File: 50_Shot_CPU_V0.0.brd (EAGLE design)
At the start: 86 x 100 mm, 74 parts, among them IC1 PIC24FJ128GA010, J1 J12, J10 22-23-2021, J11 22-23-2061, J12 A311422_nd, J13 22-23-2021, J14 22-23-2021, J3 22-23-2021, J4 22-23-2021, J5 22-23-2021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

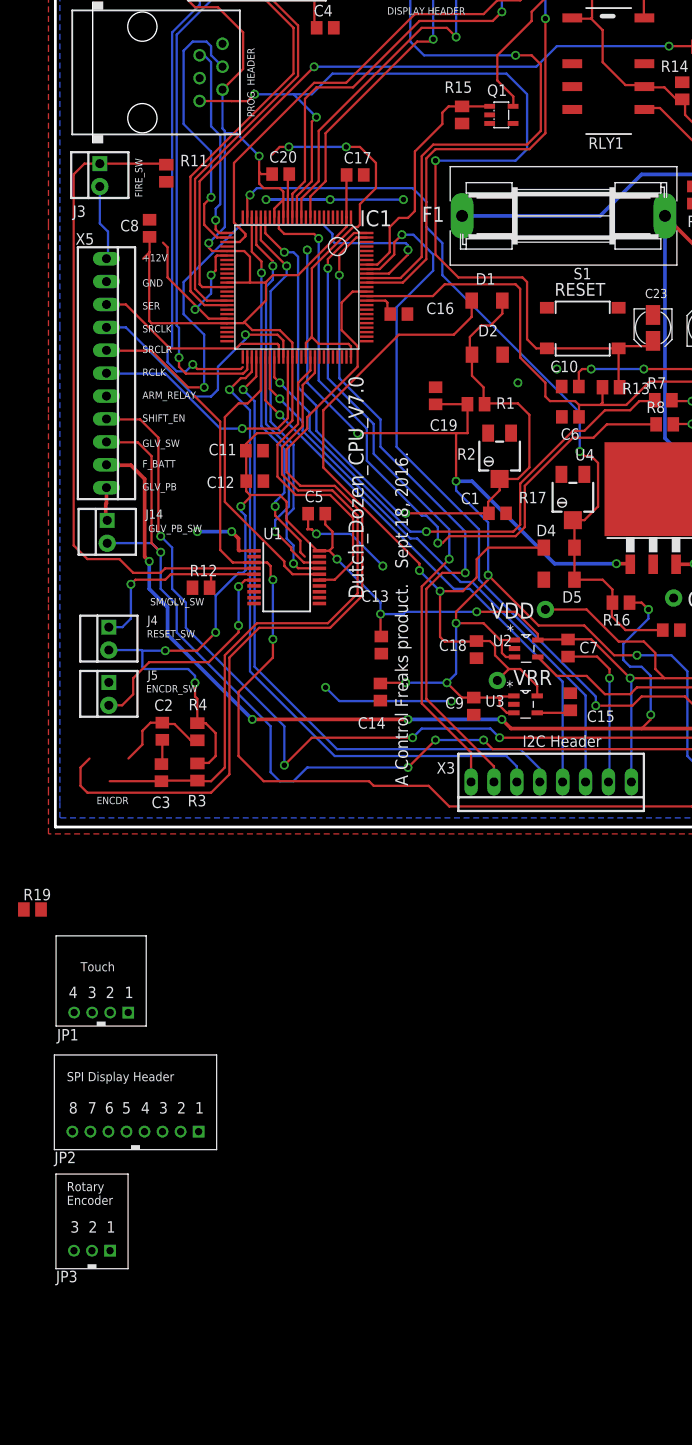
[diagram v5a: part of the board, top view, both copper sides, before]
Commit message: converted programming header
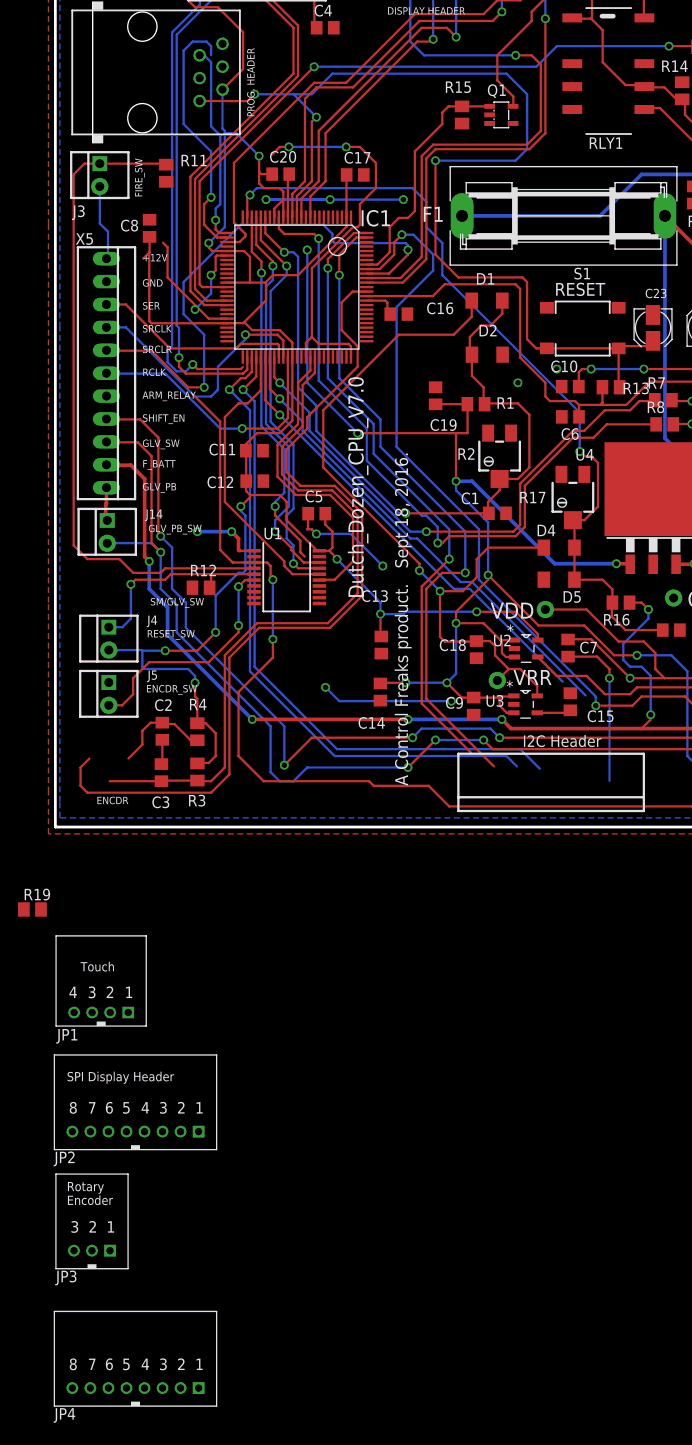
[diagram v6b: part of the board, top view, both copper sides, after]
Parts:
- removed X3: 22-23-2081, con-molex:22-23-2081
- added JP4: SHERLOCK_8PIN_RGT, Mine:SHERLOCK_8PIN-RGT
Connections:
- net 2PG_C renamed RB6_2PG_C
- net 2PG_D renamed RB7_2PG_D
- removed net SCL1-RG2: IC1.57, X3.6
- removed net SDA1-RG3: IC1.56, X3.5
- removed net VSS: C7.2, X3.7
- new net RG2_SCL1: IC1.57, JP4.6
- new net RG3_SDA1: IC1.56, JP4.5
- net GND: now also JP4.7
- net RE3: now also C7.2, JP4.2; no longer X3.2
- net RE4: now also C7.1, JP4.1; no longer X3.1
- net RF7: now also JP4.4; no longer X3.4
- net RF8: now also JP4.3; no longer X3.3
- net VDD: now also JP4.8; no longer C7.1, X3.8
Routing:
- net SCL1-RG2: track 62.8 -> 0.00 mm, vias 1 -> 0
- net SDA1-RG3: track 61.8 -> 0.00 mm, vias 1 -> 0
- net RG2_SCL1: track 0.00 -> 53.2 mm, vias 0 -> 1
- net RG3_SDA1: track 0.00 -> 50.7 mm, vias 0 -> 1
- net VSS: track 17.7 -> 0.00 mm, vias 1 -> 0
- net RE3: track 74.5 -> 90.4 mm, vias 2 -> 3
- net VDD: track 407.4 -> 392.7 mm
- net RE4: track 72.6 -> 69.4 mm
- net RB7_2PG_D: track 30.8 -> 29.0 mm
- net RF8: track 72.8 -> 71.1 mm
- net RF7: track 73.3 -> 71.8 mm

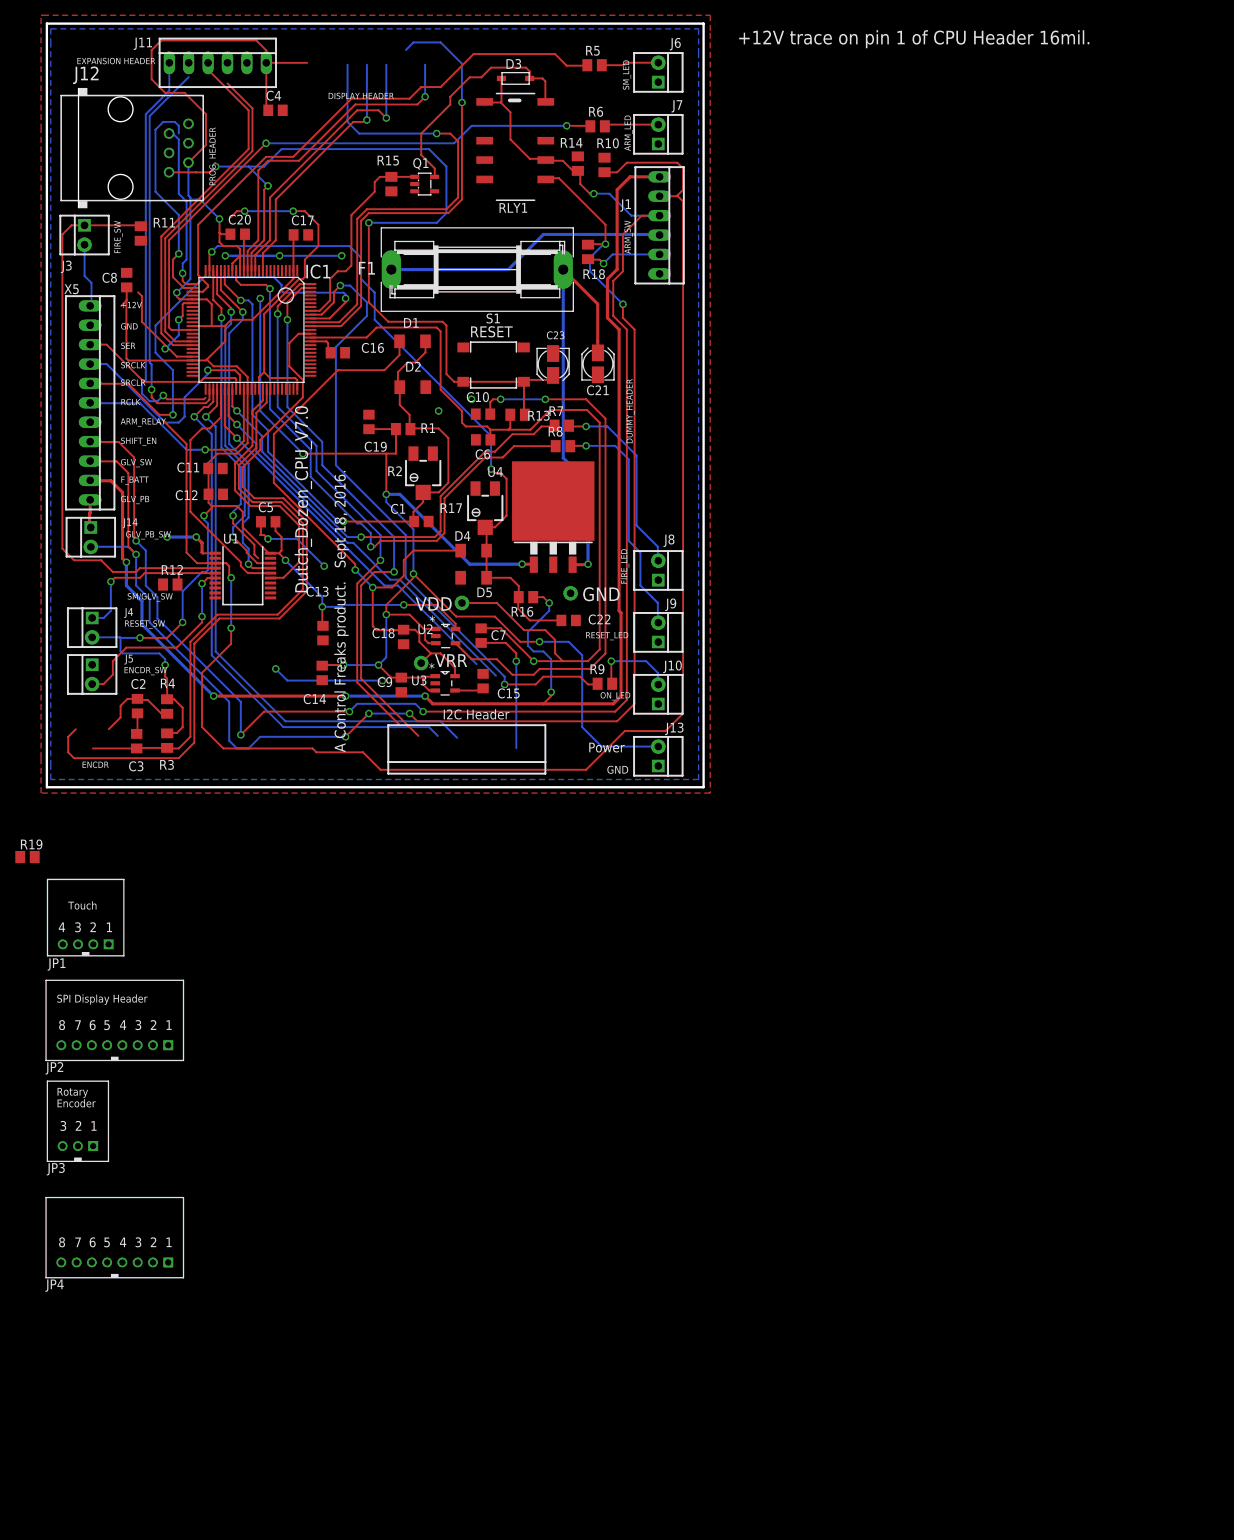
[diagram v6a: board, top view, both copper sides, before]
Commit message: converted LED headers
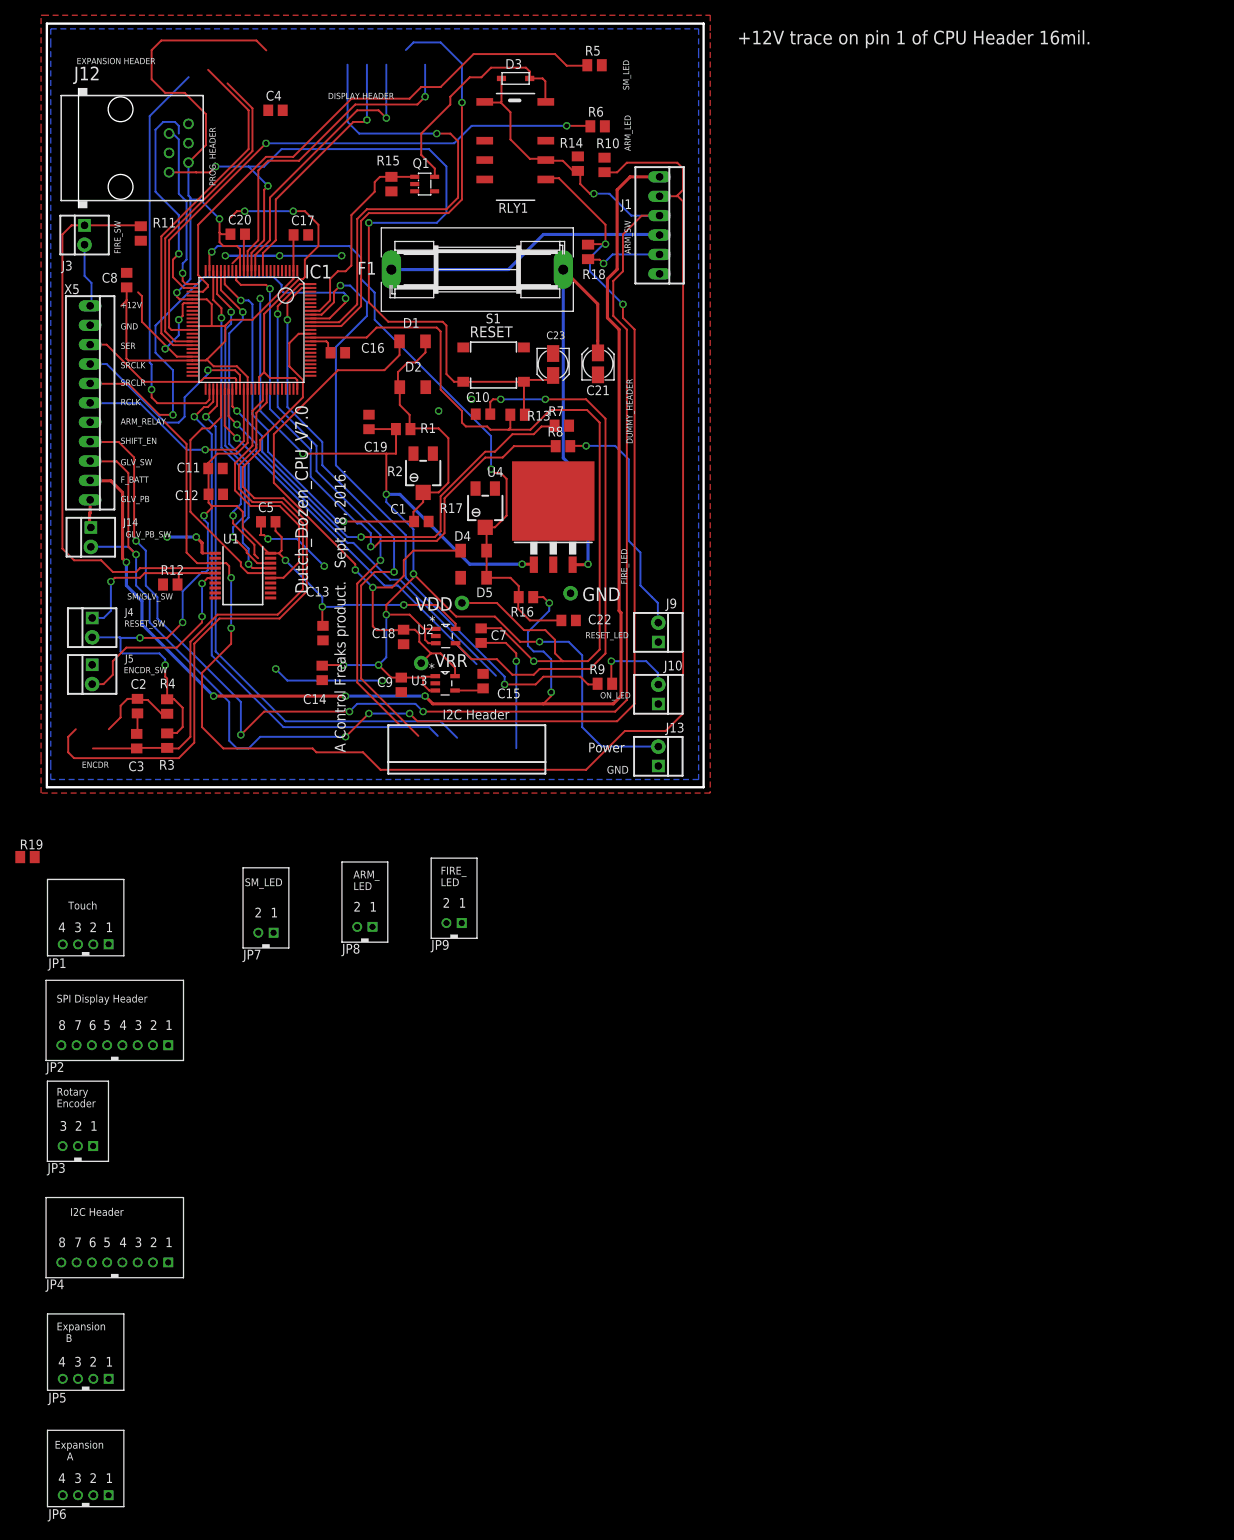
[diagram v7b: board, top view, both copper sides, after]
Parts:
- removed C6: .01uF, rcl:C0805
- removed J11: 22-23-2061, Mine:22-23-2061
- removed J6, J7, J8: 22-23-2021, Mine:22-23-2021
- added JP5, JP6: SHERLOCK_4PIN_RGT, Mine:SHERLOCK_4PIN_RGT
- added JP7, JP8, JP9: SHERLOCK_2PIN_RGT, Mine:SHERLOCK_2PIN_RGT
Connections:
- removed net ###: J11.1, J11.2, J11.3, J11.4
- removed net N$73: J8.1, R7.2
- removed net N$74: J7.1, R6.2
- removed net N$76: J6.1, R5.2
- new net N$2: JP7.1, R5.2
- new net N$6: JP8.1, R6.2
- new net N$9: JP9.1, R7.2
- new net RB0: IC1.25, JP6.3
- new net RC1: IC1.6, JP5.1
- new net RC2: IC1.7, JP5.2
- new net RC3: IC1.8, JP5.3
- new net RC4: IC1.9, JP5.4
- new net RE5: IC1.3, JP6.4
- new net RE8: IC1.18, JP6.2
- new net RE9: IC1.19, JP6.1
- net GND: now also JP7.2, JP8.2, JP9.2; no longer C6.2, J11.5, J6.2, J7.2, J8.2
- net VDD: no longer C6.1, IC1.18, J11.6
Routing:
- net ###: track 54.2 -> 0.00 mm, vias 1 -> 0
- net N$73: track 25.4 -> 0.00 mm, vias 1 -> 0
- net VDD: track 392.7 -> 377.5 mm
- net N$76: track 7.54 -> 0.00 mm
- net N$74: track 7.09 -> 0.00 mm
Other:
- board text added: "ARM_ LED"
- board text added: "Expansion A"
- board text added: "Expansion B"
- board text added: "FIRE_ LED"

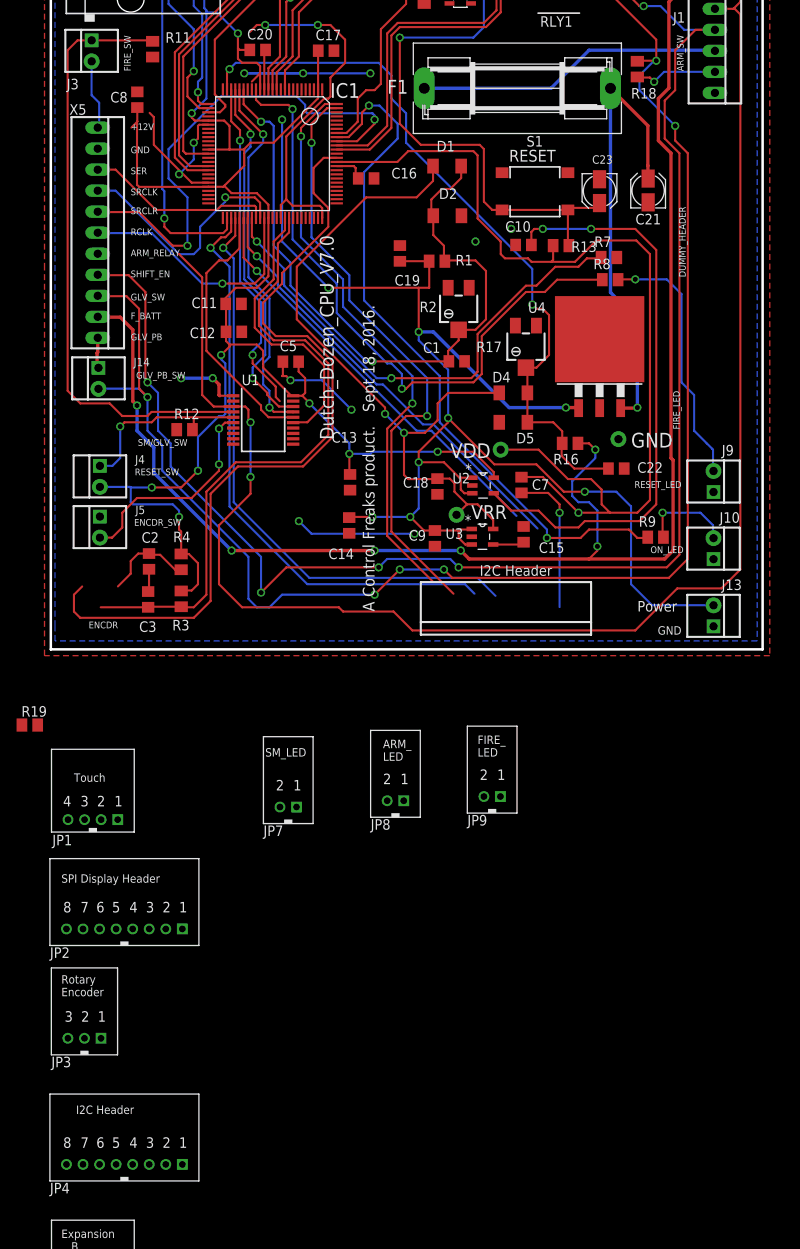
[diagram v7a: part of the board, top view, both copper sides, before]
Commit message: Added EEPROM to schematic
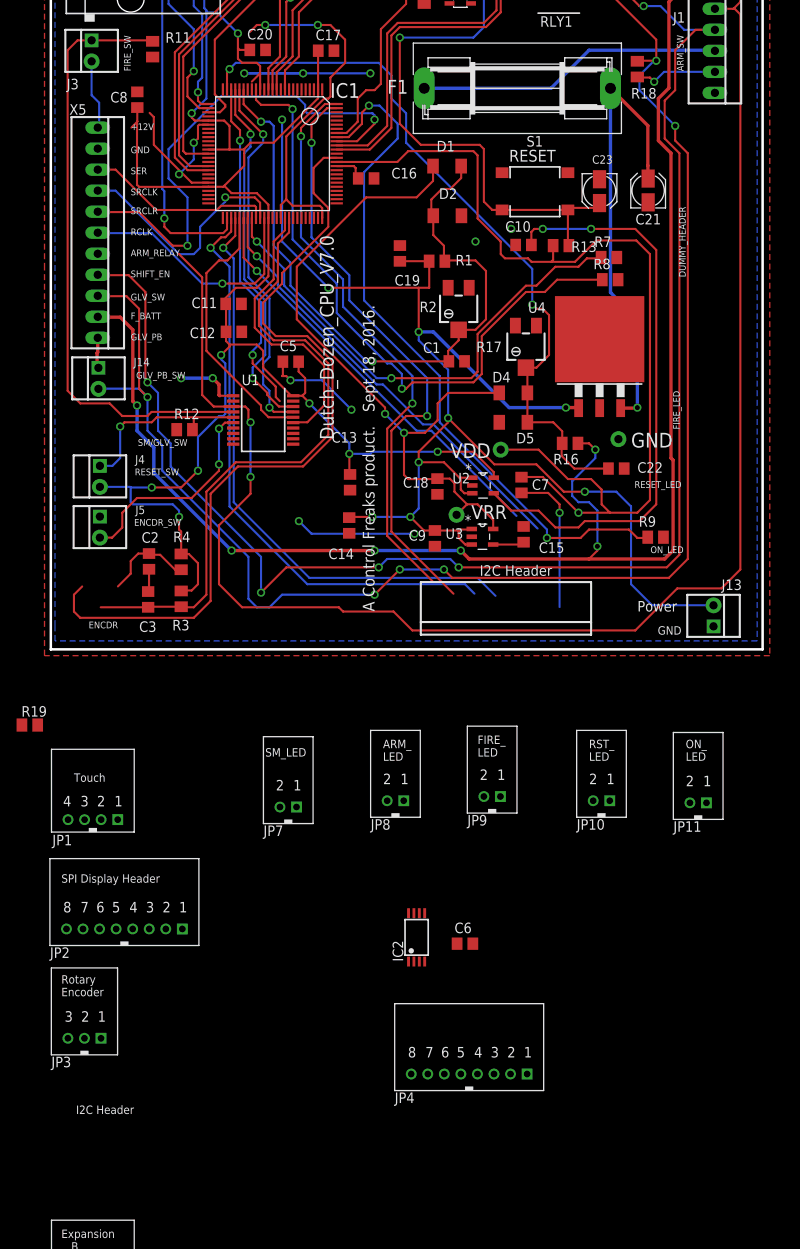
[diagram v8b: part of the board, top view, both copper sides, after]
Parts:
- removed J10, J9: 22-23-2021, Mine:22-23-2021
- added C6: .01uf, rcl:C0805
- added IC2: 93LC46ST, microchip:TSSOP8
- added JP10, JP11: SHERLOCK_2PIN_RGT, Mine:SHERLOCK_2PIN_RGT
- moved JP4 43.1 mm to (50.5, -51.3)
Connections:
- removed net N$70: J10.1, R9.2
- removed net N$72: J9.1, R8.2
- new net N$12: JP10.1, R8.2
- new net N$13: JP11.1, R9.2
- new net RB10: IC1.34, IC2.4
- new net RB11: IC1.35, IC2.3
- new net RB8: IC1.32, IC2.1
- new net RB9: IC1.33, IC2.2
- new net RG15: IC1.1, IC2.6
- net GND: now also C6.2, IC2.5, JP10.2, JP11.2; no longer J10.2, J9.2
- net VDD: now also C6.1, IC2.8
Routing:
- net N$72: track 31.4 -> 0.00 mm, vias 1 -> 0
- net N$70: track 11.3 -> 0.00 mm, vias 1 -> 0
- net GND: track 128.6 -> 124.0 mm
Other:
- board text added: "ON_ LED"
- board text added: "RST_ LED"
